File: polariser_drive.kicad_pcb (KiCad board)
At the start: 2 copper layers, 64 x 48.5 mm, 16 parts, among them J1 JACK-C-PC-10A-RA(R), J2 FlatFlex Molex, U1 SPX3819M5-L-5-0, U2 NodeMCU_Amica_R2

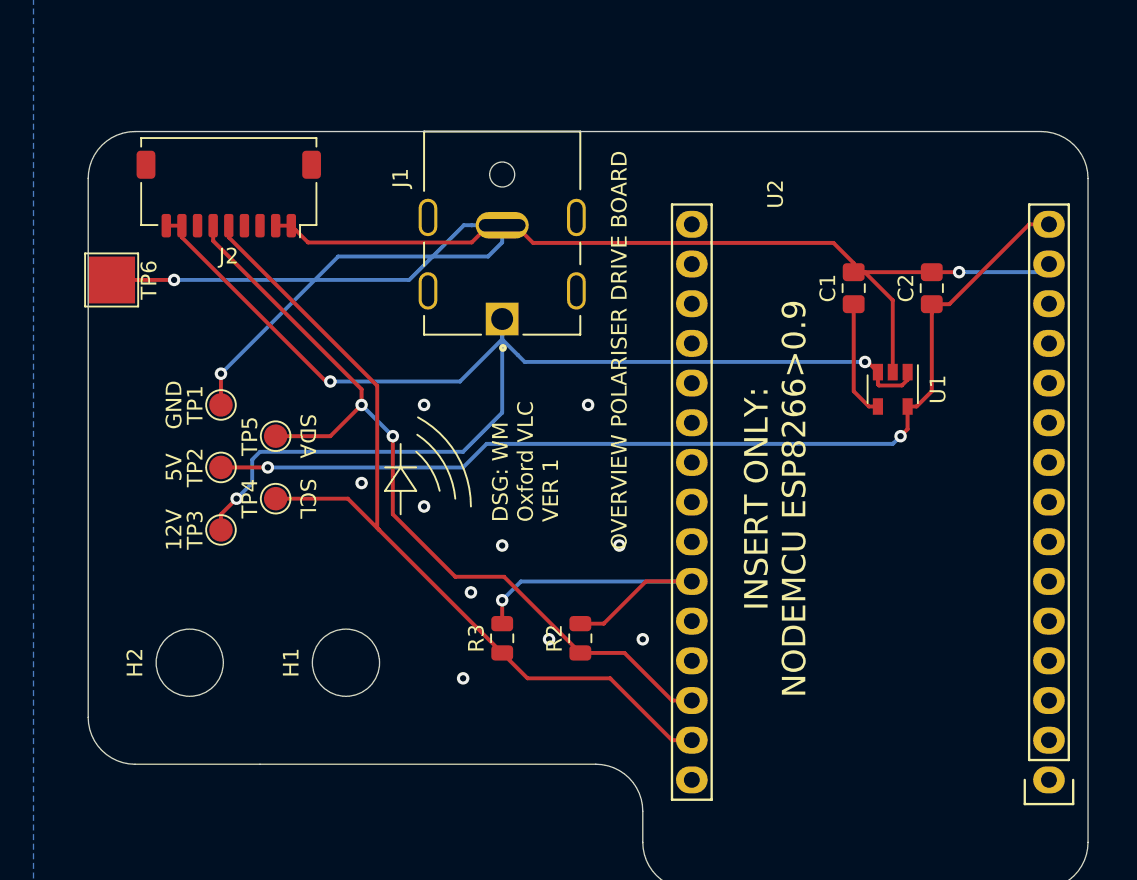
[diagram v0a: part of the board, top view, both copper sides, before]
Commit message: add another connector and configurable address lines
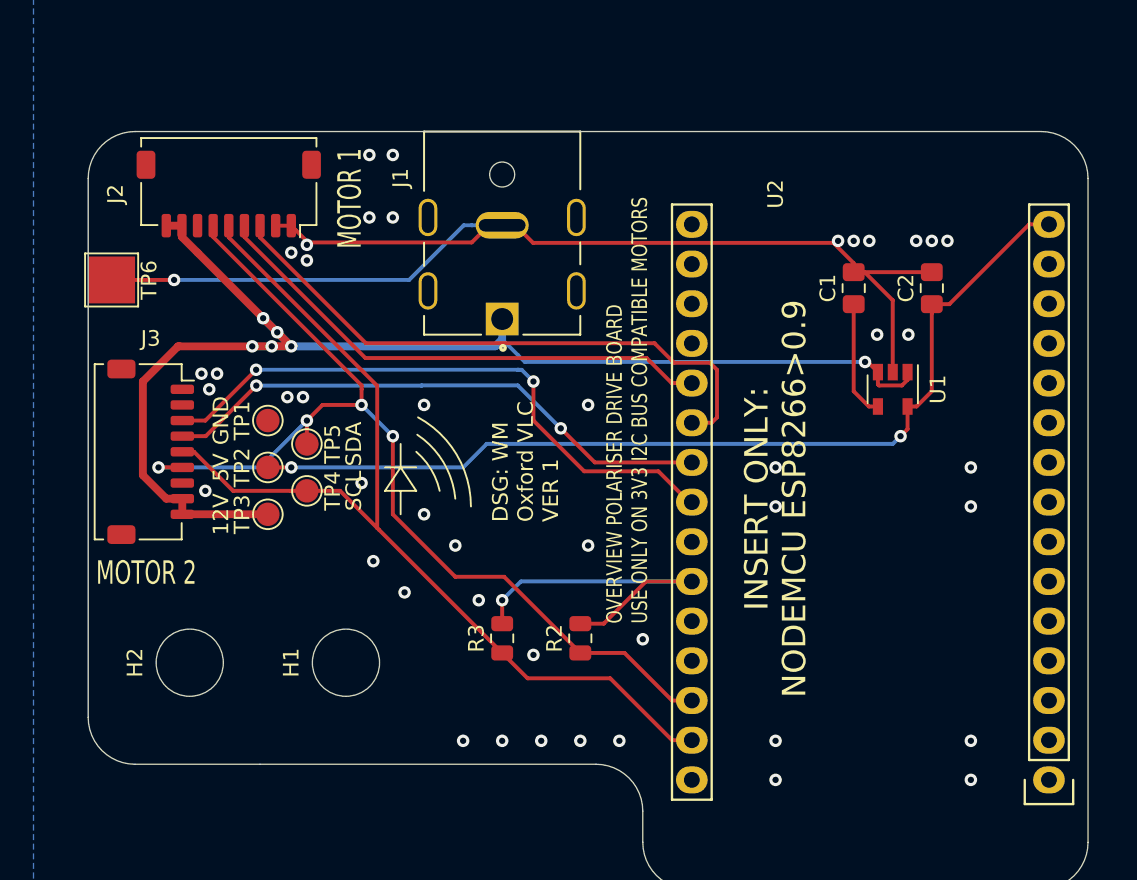
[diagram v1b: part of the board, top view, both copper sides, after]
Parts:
- added J3: FlatFlex Molex, Connector_Molex:Molex_Pico-Clasp_202396-0907_1x09-1MP_P1.00mm_Horizontal, F.Cu at (52.5, 49.0)
- R2, R3: value 5K1 -> 1K5
- moved TP1 3.16 mm to (60.0, 47.0)
- moved TP3 3.16 mm to (60.0, 53.0)
- moved TP2 3.00 mm to (60.0, 50.0)
- moved TP4 2.06 mm to (62.5, 51.5), turned to 270 degrees
- moved TP5 2.06 mm to (62.5, 48.5), turned to 270 degrees
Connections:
- J2 pad 3: Net-(J2-Pad3) -> /ADDR2A
- J2 pad 4: Net-(J2-Pad4) -> /ADDR1A
- U2 pad 20: Net-(U2-Pad20) -> /ADDR1A
- U2 pad 21: Net-(U2-Pad21) -> /ADDR2A
- U2 pad 22: Net-(U2-Pad22) -> /ADDR1B
- U2 pad 23: Net-(U2-Pad23) -> /ADDR2B
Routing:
- net /ADDR2B: track 0.00 -> 39.0 mm, vias 0 -> 2
- net /ADDR2A: track 0.00 -> 38.3 mm
- net /ADDR1B: track 0.00 -> 36.0 mm, vias 0 -> 2
- net /ADDR1A: track 0.00 -> 33.2 mm
- net GND: track 111.1 -> 79.5 mm, vias 13 -> 46
- net /SDA: track 53.6 -> 65.0 mm, vias 2 -> 4
- net /SCL: track 56.5 -> 63.5 mm
- net +5V: track 63.6 -> 60.6 mm
- net +12V: track 85.4 -> 86.1 mm, vias 3 -> 6
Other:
- net class power added: clearance 0.2, trace_width 0.5, via_dia 0.8, via_drill 0.4
- board text added: "MOTOR 1"
- board text added: "MOTOR 2"
- board text added: "OVERVIEW POLARISER DRIVE BOARD USE ONLY ON 3V3 I2C BUS COMPATIBLE MOTORS"
- board text removed: "OVERVIEW POLARISER DRIVE BOARD"

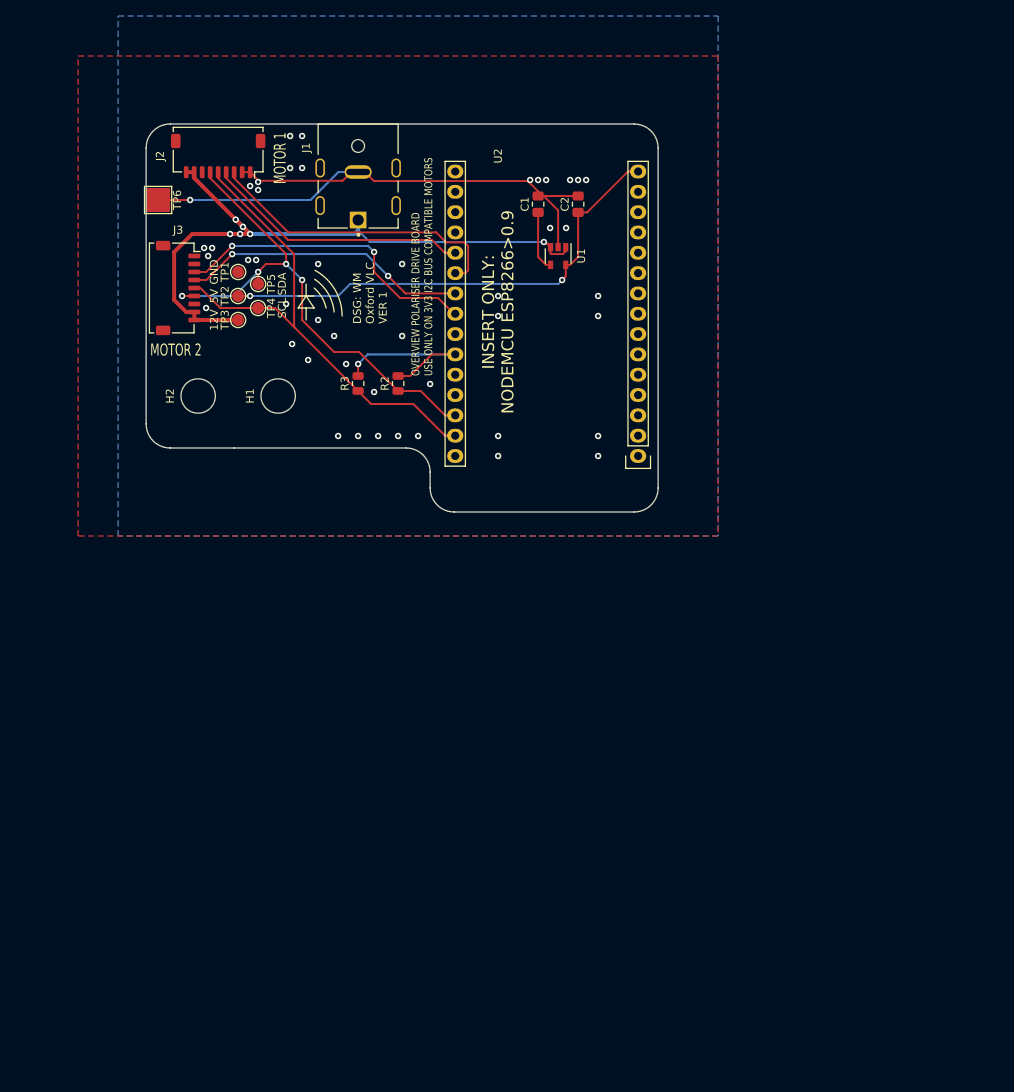
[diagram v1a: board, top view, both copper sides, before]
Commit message: stupid rookie footprint error
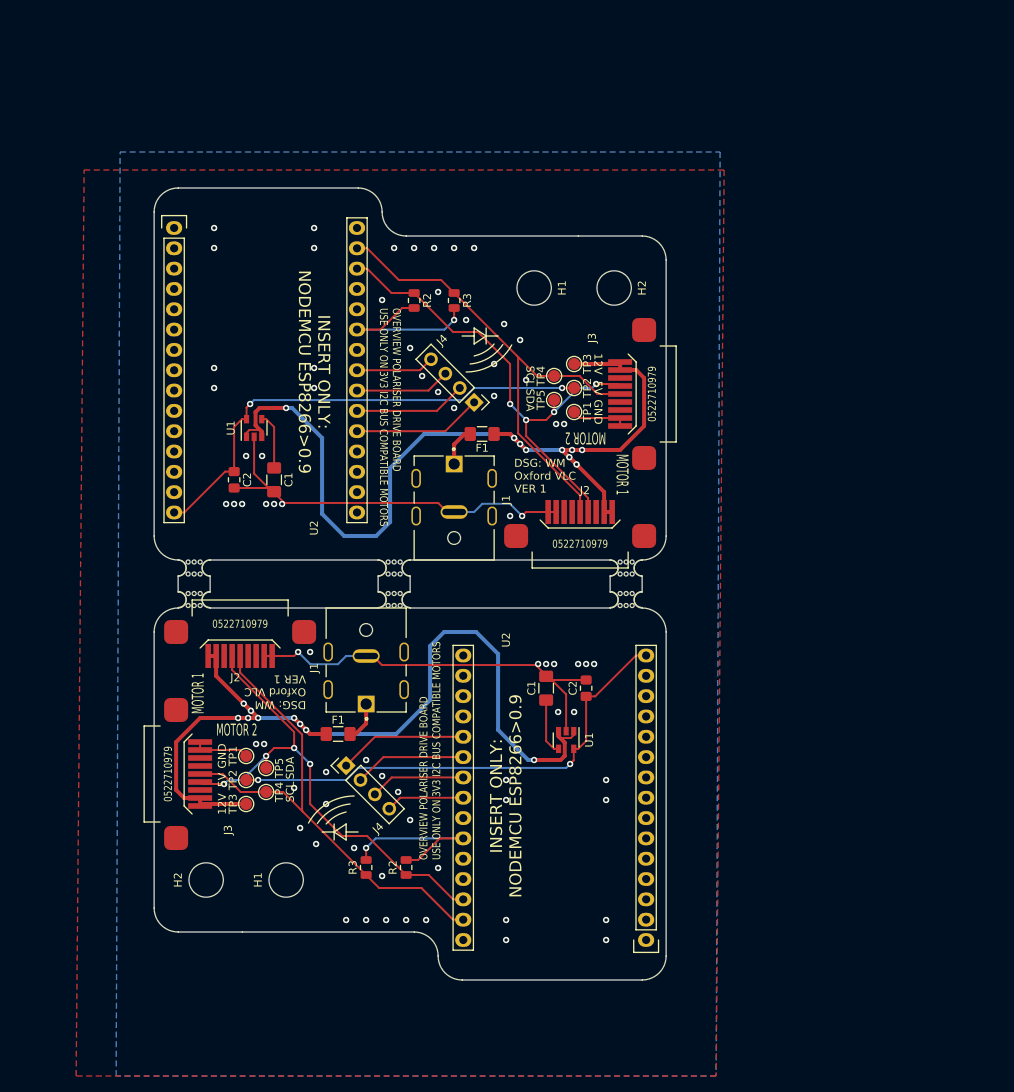
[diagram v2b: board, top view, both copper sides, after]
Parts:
- removed the J3 at (52.5, 49.0)
- removed TP6: TestPoint, TestPoint:TestPoint_Pad_3.0x3.0mm
- added C1: 0.1n, Fuse:Fuse_1206_3216Metric_Pad1.42x1.75mm_HandSolder, F.Cu at (64.5, 73.0)
- added C2: 1u, Capacitor_SMD:C_0805_2012Metric_Pad1.15x1.40mm_HandSolder, F.Cu at (59.5, 73.0)
- added F1: Fuse, Fuse:Fuse_1206_3216Metric_Pad1.42x1.75mm_HandSolder, F.Cu at (90.5, 67.2)
- added F1: Fuse, Fuse:Fuse_1206_3216Metric_Pad1.42x1.75mm_HandSolder, F.Cu at (72.5, 104.8)
- added H1: MountingHole, MountingHole:MountingHole_4.3mm_M4, F.Cu at (97.0, 49.0)
- added H2: MountingHole, MountingHole:MountingHole_4.3mm_M4, F.Cu at (107.0, 49.0)
- added J1: JACK-C-PC-10A-RA(R), globteck:GLOBTECK_JACK-C-PC-10A-RA(R), F.Cu at (87.0, 76.5)
- added J2: FlatFlex Molex, flatflex:9pos, F.Cu at (98.8, 77.0)
- added J3: FlatFlex Molex, flatflex:9pos, F.Cu at (107.8, 66.2)
- added J3: FlatFlex Molex, flatflex:9pos, F.Cu at (55.2, 105.8)
- added J4: Conn_01x04_Male, Connector_PinHeader_2.54mm:PinHeader_1x04_P2.54mm_Vertical, F.Cu at (89.5, 63.3)
- added J4: Conn_01x04_Male, Connector_PinHeader_2.54mm:PinHeader_1x04_P2.54mm_Vertical, F.Cu at (73.5, 108.7)
- added R2: 1K5, Resistor_SMD:R_0805_2012Metric, F.Cu at (82.0, 50.6)
- added R3: 1K5, Resistor_SMD:R_0805_2012Metric, F.Cu at (87.0, 50.6)
- added TP1: TestPoint, TestPoint:TestPoint_Pad_D1.5mm, F.Cu at (102.0, 64.5)
- added TP2: TestPoint, TestPoint:TestPoint_Pad_D1.5mm, F.Cu at (102.0, 61.5)
- added TP3: TestPoint, TestPoint:TestPoint_Pad_D1.5mm, F.Cu at (102.0, 58.5)
- added TP4: TestPoint, TestPoint:TestPoint_Pad_D1.5mm, F.Cu at (99.5, 60.0)
- added TP5: TestPoint, TestPoint:TestPoint_Pad_D1.5mm, F.Cu at (99.5, 63.0)
- added U1: SPX3819M5-L-5-0, Package_TO_SOT_SMD:SOT-23-5, F.Cu at (62.0, 66.5)
- added U2: NodeMCU_Amica_R2, nodemcu:NodeMCU_Amica_R2, F.Cu at (52.0, 41.5)
- added mouse-bite-2mm-slot: VAL**, Panelization:mouse-bite-2mm-slot, F.Cu at (54.5, 87.9)
- added mouse-bite-2mm-slot: VAL**, Panelization:mouse-bite-2mm-slot, F.Cu at (54.5, 84.0)
- added mouse-bite-2mm-slot: VAL**, Panelization:mouse-bite-2mm-slot, F.Cu at (79.5, 84.0)
- added mouse-bite-2mm-slot: VAL**, Panelization:mouse-bite-2mm-slot, F.Cu at (79.5, 87.9)
- added mouse-bite-2mm-slot: VAL**, Panelization:mouse-bite-2mm-slot, F.Cu at (108.5, 84.0)
- added mouse-bite-2mm-slot: VAL**, Panelization:mouse-bite-2mm-slot, F.Cu at (108.5, 87.9)
- C1: footprint Capacitor_SMD:C_0805_2012Metric_Pad1.15x1.40mm_HandSolder -> Fuse:Fuse_1206_3216Metric_Pad1.42x1.75mm_HandSolder
- J2: footprint Connector_Molex:Molex_Pico-Clasp_202396-0907_1x09-1MP_P1.00mm_Horizontal -> flatflex:9pos
- moved J2 62.9 mm to (64.2, 95.0)
- moved C1 60.5 mm to (98.5, 99.0)
- moved C2 60.5 mm to (103.5, 99.0)
- moved H1 60.5 mm to (66.0, 123.0)
- moved H2 60.5 mm to (56.0, 123.0)
- moved J1 60.5 mm to (76.0, 95.5)
- moved R2 60.5 mm to (81.0, 121.4)
- moved R3 60.5 mm to (76.0, 121.4)
- moved TP1 60.5 mm to (61.0, 107.5)
- moved TP2 60.5 mm to (61.0, 110.5)
- moved TP3 60.5 mm to (61.0, 113.5)
- moved TP4 60.5 mm to (63.5, 112.0)
- moved TP5 60.5 mm to (63.5, 109.0)
- moved U1 60.5 mm to (101.0, 105.5)
- moved U2 60.5 mm to (111.0, 130.5)
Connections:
- J1 pad 1: +12V -> Net-(F1-Pad1)
- J2 pad 3: /ADDR2A -> Net-(J2-Pad3)
- J2 pad 4: /ADDR1A -> Net-(J2-Pad4)
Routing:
- net +12V: track 86.1 -> 233.0 mm, vias 6 -> 18
- net /SCL: track 63.5 -> 126.0 mm
- net +5V: track 60.6 -> 121.1 mm, vias 2 -> 4
- net /SDA: track 65.0 -> 123.7 mm, vias 4 -> 8
- net GND: track 79.5 -> 119.3 mm, vias 46 -> 74
- net Net-(R2-Pad2): track 22.4 -> 44.8 mm, vias 1 -> 2
- net /ADDR2B: track 39.0 -> 19.6 mm, vias 2 -> 0
- net /ADDR1B: track 36.0 -> 23.8 mm, vias 2 -> 0
- net /ADDR2A: track 38.3 -> 28.1 mm
- net Net-(F1-Pad1): track 0.00 -> 10.0 mm
- net Net-(C1-Pad1): track 7.53 -> 15.1 mm
- net /ADDR1A: track 33.2 -> 32.3 mm
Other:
- board size 64 x 48.5 mm -> 64 x 99 mm

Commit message: board finished
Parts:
- removed the C1 at (64.5, 73.0)
- removed the C2 at (59.5, 73.0)
- removed the F1 at (90.5, 67.2)
- removed the H1 at (97.0, 49.0)
- removed the H2 at (107.0, 49.0)
- removed the J1 at (87.0, 76.5)
- removed the J2 at (98.8, 77.0)
- removed the J3 at (107.8, 66.2)
- removed J4 (x2): Conn_01x04_Male, Connector_PinHeader_2.54mm:PinHeader_1x04_P2.54mm_Vertical
- removed the R2 at (82.0, 50.6)
- removed the R3 at (87.0, 50.6)
- removed the TP1 at (102.0, 64.5)
- removed the TP2 at (102.0, 61.5)
- removed the TP3 at (102.0, 58.5)
- removed the TP4 at (99.5, 60.0)
- removed the TP5 at (99.5, 63.0)
- removed the U1 at (62.0, 66.5)
- removed the U2 at (52.0, 41.5)
- removed mouse-bite-2mm-slot (x6): VAL**, Panelization:mouse-bite-2mm-slot
- F1: footprint Fuse:Fuse_1206_3216Metric_Pad1.42x1.75mm_HandSolder -> Resistor_THT:R_Axial_DIN0309_L9.0mm_D3.2mm_P12.70mm_Horizontal
- TP4, TP5: footprint TestPoint:TestPoint_Pad_D1.5mm -> Connector_PinHeader_2.54mm:PinHeader_1x01_P2.54mm_Vertical
- moved F1 13.1 mm to (80.0, 115.5), turned to 135 degrees
- turned TP4 to 180 degrees
- turned TP5 to 0 degrees
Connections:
- J2 pad 1: GND -> +12V
- J2 pad 2: GND -> +12V
- J2 pad 4: Net-(J2-Pad4) -> /SDA
- J2 pad 6: /SDA -> Net-(J2-Pad6)
- J2 pad 8: +12V -> GND
- J2 pad 9: +12V -> GND
- J3 pad 1: GND -> +12V
- J3 pad 2: GND -> +12V
- J3 pad 4: Net-(J3-Pad4) -> /SDA
- J3 pad 6: /SDA -> Net-(J3-Pad6)
- J3 pad 8: +12V -> GND
- J3 pad 9: +12V -> GND
- U2 pad 20: /ADDR1A -> Net-(U2-Pad20)
- U2 pad 21: /ADDR2A -> Net-(U2-Pad21)
- U2 pad 22: /ADDR1B -> Net-(U2-Pad22)
- U2 pad 23: /ADDR2B -> Net-(U2-Pad23)
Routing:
- net +12V: track 233.0 -> 97.4 mm, vias 18 -> 8
- net GND: track 119.3 -> 41.8 mm, vias 74 -> 42
- net /SDA: track 123.7 -> 59.6 mm, vias 8 -> 4
- net /SCL: track 126.0 -> 63.0 mm
- net +5V: track 121.1 -> 60.6 mm, vias 4 -> 2
- net /ADDR1A: track 32.3 -> 0.00 mm
- net /ADDR2A: track 28.1 -> 0.00 mm
- net /ADDR1B: track 23.8 -> 0.00 mm
- net Net-(R2-Pad2): track 44.8 -> 22.4 mm, vias 2 -> 1
- net /ADDR2B: track 19.6 -> 0.00 mm
- net Net-(C1-Pad1): track 15.1 -> 7.53 mm
- net Net-(F1-Pad1): track 10.0 -> 16.9 mm
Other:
- board size 64 x 99 mm -> 64 x 46.5 mm
- board text added: "3"
- board text added: "DSG: WM Oxford VLC VER 3"
- board text added: "JLCJLCJLCJLC"
- board text removed: "DSG: WM Oxford VLC VER 1"
